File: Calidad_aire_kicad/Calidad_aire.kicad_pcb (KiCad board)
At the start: 2 copper layers, 1 part, among them U1 DOIT-ESP32-DEVKIT-V1

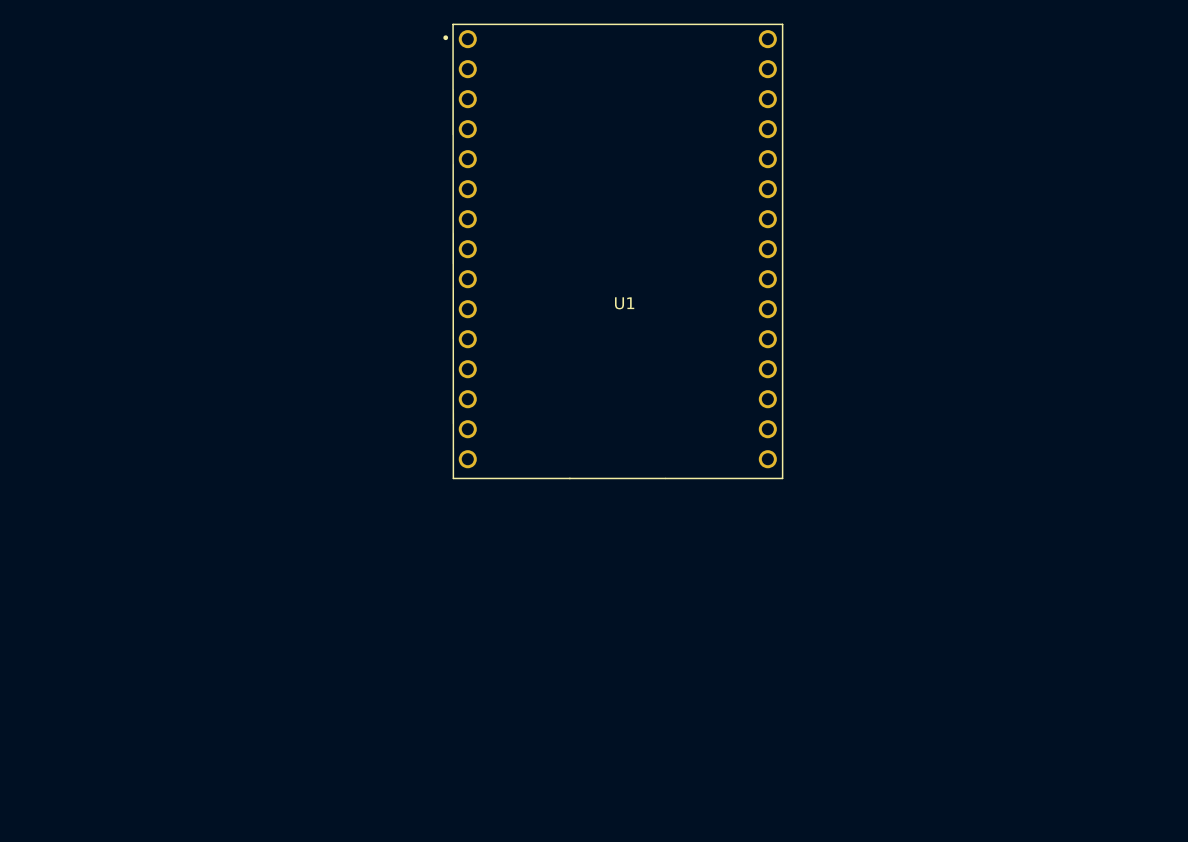
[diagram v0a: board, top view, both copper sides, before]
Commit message: design of the footprints for the components
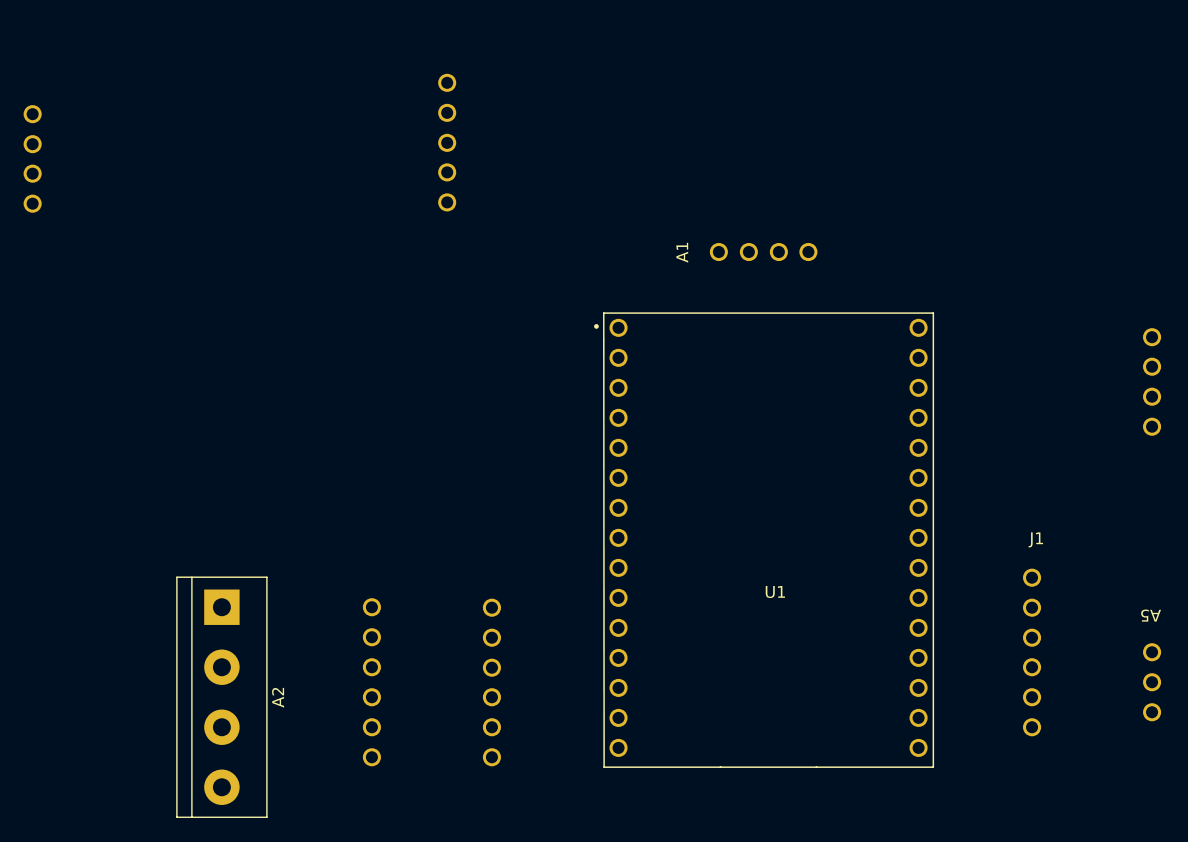
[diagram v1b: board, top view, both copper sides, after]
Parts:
- added A1: ~, footprint_project:MQ_135, F.Cu at (112.8, 53.8)
- added A2: ~, TerminalBlock:TerminalBlock_bornier-4_P5.08mm, F.Cu at (67.3, 83.8)
- added A3: ~, footprint_project:MH_Z19B, F.Cu at (67.7, 45.2)
- added A4: ~, footprint_project:OLED_128064, F.Cu at (146.1, 65.0)
- added A5: ~, footprint_project:DHT22, F.Cu at (146.0, 90.2)
- added J1: Micro_SD_Card, footprint_project:microSD, F.Cu at (135.9, 85.2)
- added U2: ~, footprint_project:conv_niv_log, F.Cu at (84.6, 90.0)
- moved U1 27.6 mm to (114.4, 75.2)

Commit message: PCB design actualization
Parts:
- added BT1: Battery_Cell, TerminalBlock:TerminalBlock_bornier-2_P5.08mm, F.Cu at (156.8, 88.3)
- added R1: 2K, Resistor_THT:R_Axial_DIN0414_L11.9mm_D4.5mm_P15.24mm_Horizontal, F.Cu at (199.9, 80.9)
- added R2: 1K, Resistor_THT:R_Axial_DIN0414_L11.9mm_D4.5mm_P15.24mm_Horizontal, F.Cu at (192.2, 96.1)
- added U3: ~, footprint_project:USB_TP4056, F.Cu at (170.4, 105.3)
- moved A3 203.6 mm to (253.0, 129.6), turned to 180 degrees
- moved A2 197.8 mm to (264.6, 97.4)
- moved U2 136.1 mm to (213.8, 132.8)
- moved J1 110.9 mm to (244.3, 108.7), turned to 180 degrees
- moved A5 104.7 mm to (250.6, 86.0), turned to -90 degrees
- moved A4 94.0 mm to (232.8, 101.3), turned to 0 degrees
- moved U1 87.8 mm to (191.0, 118.0)
- moved A1 79.5 mm to (180.6, 95.2)
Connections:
- A2 pad 1: TX0_3V -> TX0_5V
- A2 pad 2: RX0_3V -> RX0_5V
- A3 pad 1: TX2_3V -> TX2_5V
- A3 pad 2: RX2_3V -> RX2_5V
- U1 pad 12: unconnected-(U1-GPIO12_ADC2-CH5_HSPI-MISO_RTC-GPIO15-Pad12) -> RX0_3V
- U1 pad 13: unconnected-(U1-GPIO13_ADC2-CH4_HSPI-MOSI_RTC-GPIO14-Pad13) -> TX0_3V
- U1 pad 20: unconnected-(U1-GPIO4_ADC2-CH0_RTC-GPIO10-Pad20) -> 3.3V
- U1 pad 21: RX2_5V -> RX2_3V
- U1 pad 22: TX2_5V -> TX2_3V
- U1 pad 27: RX0_5V -> unconnected-(U1-GPIO3__UART0-RX-Pad27)
- U1 pad 28: TX0_5V -> unconnected-(U1-GPIO1_UART0-TX-Pad28)
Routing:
- net 5V: track 0.00 -> 281.0 mm
- net 3.3V: track 0.00 -> 107.8 mm
- net DHT_22: track 0.00 -> 95.0 mm
- net TX0_5V: track 0.00 -> 64.8 mm
- net RX0_5V: track 0.00 -> 61.5 mm
- net Net-(BT1-+): track 0.00 -> 57.7 mm
- net TX0_3V: track 0.00 -> 57.2 mm
- net RX0_3V: track 0.00 -> 53.3 mm
- net SD_MISO: track 0.00 -> 45.7 mm
- net SD_CLK: track 0.00 -> 44.7 mm
- net SD_SS: track 0.00 -> 44.7 mm
- net SD_MOSI: track 0.00 -> 43.3 mm
- net AO_MQ_135: track 0.00 -> 34.6 mm
- net SDA: track 0.00 -> 33.1 mm
- net SCK: track 0.00 -> 31.0 mm
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- added copper zone on F.Cu, net GND

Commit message: adjustment to the PCB design
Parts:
- moved BT1 101.0 mm to (255.9, 68.6), turned to 180 degrees
- moved U3 72.2 mm to (238.8, 82.2), turned to 180 degrees
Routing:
- net 5V: track 281.0 -> 302.8 mm
- net TX0_3V: track 57.2 -> 65.4 mm
- net RX0_3V: track 53.3 -> 56.6 mm
- net Net-(BT1-+): track 57.7 -> 60.6 mm
- net 3.3V: track 107.8 -> 109.8 mm
- net DHT_22: track 95.0 -> 96.1 mm
- net RX2_3V: track 18.6 -> 17.6 mm
- net RX0_5V: track 61.5 -> 62.1 mm

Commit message: change
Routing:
- removed copper zone on F.Cu, net GND
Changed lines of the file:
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@@
 			(psnegative no)
 			(psa4output no)
-			(plotreference yes)
-			(plotvalue yes)
-			(plotfptext yes)
+			(plotreference no)
+			(plotvalue no)
+			(plotfptext no)
 			(plotinvisibletext no)
 			(sketchpadsonfab no)
 			(subtractmaskfromsilk no)
-			(outputformat 4)
-			(mirror yes)
+			(outputformat 1)
+			(mirror no)
 			(drillshape 0)
 			(scaleselection 1)
-			(outputdirectory "./")
+			(outputdirectory "Gerber/")
 		)
 	)
@@
 		(net 34)
 	)
-	(zone
-		(net 17)
-		(net_name "GND")
-		(layer "F.Cu")
-		(hatch edge 0.5)
-		(connect_pads
-			(clearance 0.5)
-		)
-		(min_thickness 0.25)
-		(filled_areas_thickness no)
-		(fill yes
-			(thermal_gap 0.5)
-			(thermal_bridge_width 0.5)
-		)
-		(polygon
-			(pts
-				(xy 171.704 151.384) (xy 171.704 53.34) (xy 273.05 53.34) (xy 273.05 151.384)
-			)
-		)
-	)
 )
